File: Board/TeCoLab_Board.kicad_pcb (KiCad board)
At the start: 2 copper layers, 95.1 x 93.8 mm, 61 parts, among them J1 Jack, J2 Supply_Terminal, J3 DC Cooler, Q1 BC337, Q2 TIP122, Q3 TIP122, U1 DS18B20, U2 PC817, U3 DS18B20, U4 DS18B20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

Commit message: PCB: Mounting holes updated to 7 mm. TeCoLab logo resized to 70 percent of the previous size.
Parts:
- removed the G*** at (141.3, 106.6)
- added G***: LOGO, logo:logo, B.Cu at (141.5, 106.2)

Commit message: Schematic: swap of the two labels named Sensor1 and Sensor2. This changes nothing in the PCB layout, but the files were checked as well and saved, generating a new version of them too. Firmware: changed the define of the pin of each sensor, according to the previously mentioned change in the schematic.
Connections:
- A1 pad 11: Sensor_1 -> Sensor_2
- A1 pad 12: Sensor_2 -> Sensor_1
- R5 pad 1: Sensor_2 -> Sensor_1
- R8 pad 1: Sensor_1 -> Sensor_2
- TP6 pad 1: Sensor_1 -> Sensor_2
- TP7 pad 1: Sensor_2 -> Sensor_1
- U3 pad 2: Sensor_2 -> Sensor_1
- U4 pad 2: Sensor_1 -> Sensor_2
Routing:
- net Sensor_2: track 97.9 -> 43.7 mm
- net Sensor_1: track 43.7 -> 97.9 mm
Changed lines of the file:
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@@
       (net 43 "Net-(A1-Pad26)"))
     (pad 11 thru_hole oval (at 0 25.4 180) (size 1.6 1.6) (drill 0.8) (layers *.Cu *.Mask)
-      (net 7 Sensor_1))
+      (net 9 Sensor_2))
     (pad 27 thru_hole oval (at 15.24 7.62 180) (size 1.6 1.6) (drill 0.8) (layers *.Cu *.Mask)
       (net 8 +5V))
     (pad 12 thru_hole oval (at 0 27.94 180) (size 1.6 1.6) (drill 0.8) (layers *.Cu *.Mask)
-      (net 9 Sensor_2))
+      (net 7 Sensor_1))
     (pad 28 thru_hole oval (at 15.24 5.08 180) (size 1.6 1.6) (drill 0.8) (layers *.Cu *.Mask)
       (net 44 "Net-(A1-Pad28)"))
@@
       (net 8 +5V))
     (pad 1 thru_hole circle (at 0 0 90) (size 1.6 1.6) (drill 0.8) (layers *.Cu *.Mask)
-      (net 9 Sensor_2))
+      (net 7 Sensor_1))
     (model ${KISYS3DMOD}/Resistor_THT.3dshapes/R_Axial_DIN0207_L6.3mm_D2.5mm_P7.62mm_Horizontal.wrl
       (at (xyz 0 0 0))
@@
     )
     (pad 1 thru_hole circle (at 0 0 270) (size 1.6 1.6) (drill 0.8) (layers *.Cu *.Mask)
-      (net 7 Sensor_1))
+      (net 9 Sensor_2))
     (pad 2 thru_hole oval (at 7.62 0 270) (size 1.6 1.6) (drill 0.8) (layers *.Cu *.Mask)
       (net 8 +5V))
@@
     (fp_arc (start 1.27 0) (end 1.27 -2.6) (angle 135) (layer F.SilkS) (width 0.12))
     (pad 2 thru_hole oval (at 1.27 0 90) (size 1.05 1.5) (drill 0.75) (layers *.Cu *.Mask)
-      (net 9 Sensor_2))
+      (net 7 Sensor_1))
     (pad 3 thru_hole oval (at 2.54 0 90) (size 1.05 1.5) (drill 0.75) (layers *.Cu *.Mask)
       (net 8 +5V))
@@
       (net 8 +5V))
     (pad 2 thru_hole oval (at 1.27 0 270) (size 1.05 1.5) (drill 0.75) (layers *.Cu *.Mask)
-      (net 7 Sensor_1))
+      (net 9 Sensor_2))
     (model ${KISYS3DMOD}/Package_TO_SOT_THT.3dshapes/TO-92_Inline.wrl
       (at (xyz 0 0 0))
@@
     )
     (pad 1 thru_hole circle (at 0 0) (size 1 1) (drill 0.5) (layers *.Cu *.Mask)
-      (net 7 Sensor_1))
+      (net 9 Sensor_2))
   )
   (module TestPoint:TestPoint_THTPad_D1.0mm_Drill0.5mm (layer F.Cu)
@@
     (fp_circle (center 0 0) (end 0 0.7) (layer F.SilkS) (width 0.12))
     (pad 1 thru_hole circle (at 0 0) (size 1 1) (drill 0.5) (layers *.Cu *.Mask)
-      (net 9 Sensor_2))
+      (net 7 Sensor_1))
   )
   (module MountingHole:MountingHole_6mm (layer F.Cu)
@@
   (segment (start 196.7484 61.77284) (end 191.20108 67.32016) (width 0.2) (layer F.Cu) (net 6))
   (segment (start 196.7484 60.82284) (end 196.7484 61.77284) (width 0.2) (layer F.Cu) (net 6))
-  (segment (start 181.93004 51.36388) (end 181.89956 51.3334) (width 0.2) (layer B.Cu) (net 7))
-  (segment (start 184.7342 51.3334) (end 184.76468 51.36388) (width 0.2) (layer B.Cu) (net 7))
-  (segment (start 181.89956 51.3334) (end 184.7342 51.3334) (width 0.2) (layer B.Cu) (net 7))
-  (segment (start 181.89956 51.3334) (end 179.05476 51.3334) (width 0.2) (layer F.Cu) (net 7))
-  (segment (start 179.05476 51.3334) (end 167.34536 39.624) (width 0.2) (layer F.Cu) (net 7))
-  (segment (start 163.18992 39.624) (end 162.04184 40.77208) (width 0.2) (layer F.Cu) (net 7))
-  (segment (start 167.34536 39.624) (end 163.18992 39.624) (width 0.2) (layer F.Cu) (net 7))
-  (segment (start 161.241841 41.572079) (end 161.221521 41.572079) (width 0.2) (layer F.Cu) (net 7))
-  (segment (start 162.04184 40.77208) (end 161.241841 41.572079) (width 0.2) (layer F.Cu) (net 7))
-  (segment (start 158.21152 44.58208) (end 148.07184 44.58208) (width 0.2) (layer F.Cu) (net 7))
-  (segment (start 161.221521 41.572079) (end 158.21152 44.58208) (width 0.2) (layer F.Cu) (net 7))
+  (segment (start 181.93004 51.36388) (end 181.89956 51.3334) (width 0.2) (layer B.Cu) (net 9))
+  (segment (start 184.7342 51.3334) (end 184.76468 51.36388) (width 0.2) (layer B.Cu) (net 9))
+  (segment (start 181.89956 51.3334) (end 184.7342 51.3334) (width 0.2) (layer B.Cu) (net 9))
+  (segment (start 181.89956 51.3334) (end 179.05476 51.3334) (width 0.2) (layer F.Cu) (net 9))
+  (segment (start 179.05476 51.3334) (end 167.34536 39.624) (width 0.2) (layer F.Cu) (net 9))
+  (segment (start 163.18992 39.624) (end 162.04184 40.77208) (width 0.2) (layer F.Cu) (net 9))
+  (segment (start 167.34536 39.624) (end 163.18992 39.624) (width 0.2) (layer F.Cu) (net 9))
+  (segment (start 161.241841 41.572079) (end 161.221521 41.572079) (width 0.2) (layer F.Cu) (net 9))
+  (segment (start 162.04184 40.77208) (end 161.241841 41.572079) (width 0.2) (layer F.Cu) (net 9))
+  (segment (start 158.21152 44.58208) (end 148.07184 44.58208) (width 0.2) (layer F.Cu) (net 9))
+  (segment (start 161.221521 41.572079) (end 158.21152 44.58208) (width 0.2) (layer F.Cu) (net 9))
   (segment (start 136.92124 50.01768) (end 146.29384 50.01768) (width 0.2) (layer B.Cu) (net 8))
   (segment (start 148.07184 48.23968) (end 148.07184 45.85208) (width 0.2) (layer B.Cu) (net 8) (status 20))
@@
   (segment (start 129.93624 43.31208) (end 134.10184 43.31208) (width 0.2) (layer B.Cu) (net 8))
   (segment (start 128.66624 42.04208) (end 129.93624 43.31208) (width 0.2) (layer B.Cu) (net 8))
-  (segment (start 181.95036 48.7426) (end 181.89956 48.7934) (width 0.2) (layer B.Cu) (net 9))
-  (segment (start 120.63984 48.39208) (end 120.63984 46.97476) (width 0.2) (layer B.Cu) (net 9))
-  (segment (start 123.03252 44.58208) (end 134.10184 44.58208) (width 0.2) (layer B.Cu) (net 9))
-  (segment (start 120.63984 46.97476) (end 123.03252 44.58208) (width 0.2) (layer B.Cu) (net 9))
-  (segment (start 181.92496 48.768) (end 181.89956 48.7934) (width 0.2) (layer B.Cu) (net 9))
-  (segment (start 184.82564 48.768) (end 181.92496 48.768) (width 0.2) (layer B.Cu) (net 9))
-  (segment (start 178.36896 48.7934) (end 181.89956 48.7934) (width 0.2) (layer B.Cu) (net 9))
-  (segment (start 119.85244 37.92728) (end 167.50284 37.92728) (width 0.2) (layer B.Cu) (net 9))
-  (segment (start 118.76024 39.01948) (end 119.85244 37.92728) (width 0.2) (layer B.Cu) (net 9))
-  (segment (start 118.76024 47.89424) (end 118.76024 39.01948) (width 0.2) (layer B.Cu) (net 9))
-  (segment (start 167.50284 37.92728) (end 178.36896 48.7934) (width 0.2) (layer B.Cu) (net 9))
-  (segment (start 119.25808 48.39208) (end 118.76024 47.89424) (width 0.2) (layer B.Cu) (net 9))
-  (segment (start 120.63984 48.39208) (end 119.25808 48.39208) (width 0.2) (layer B.Cu) (net 9))
+  (segment (start 181.95036 48.7426) (end 181.89956 48.7934) (width 0.2) (layer B.Cu) (net 7))
+  (segment (start 120.63984 48.39208) (end 120.63984 46.97476) (width 0.2) (layer B.Cu) (net 7))
+  (segment (start 123.03252 44.58208) (end 134.10184 44.58208) (width 0.2) (layer B.Cu) (net 7))
+  (segment (start 120.63984 46.97476) (end 123.03252 44.58208) (width 0.2) (layer B.Cu) (net 7))
+  (segment (start 181.92496 48.768) (end 181.89956 48.7934) (width 0.2) (layer B.Cu) (net 7))
+  (segment (start 184.82564 48.768) (end 181.92496 48.768) (width 0.2) (layer B.Cu) (net 7))
+  (segment (start 178.36896 48.7934) (end 181.89956 48.7934) (width 0.2) (layer B.Cu) (net 7))
+  (segment (start 119.85244 37.92728) (end 167.50284 37.92728) (width 0.2) (layer B.Cu) (net 7))
+  (segment (start 118.76024 39.01948) (end 119.85244 37.92728) (width 0.2) (layer B.Cu) (net 7))
+  (segment (start 118.76024 47.89424) (end 118.76024 39.01948) (width 0.2) (layer B.Cu) (net 7))
+  (segment (start 167.50284 37.92728) (end 178.36896 48.7934) (width 0.2) (layer B.Cu) (net 7))
+  (segment (start 119.25808 48.39208) (end 118.76024 47.89424) (width 0.2) (layer B.Cu) (net 7))
+  (segment (start 120.63984 48.39208) (end 119.25808 48.39208) (width 0.2) (layer B.Cu) (net 7))
   (segment (start 157.309921 46.069361) (end 157.309921 46.068081) (width 0.2) (layer B.Cu) (net 10))
   (segment (start 158.10992 46.86936) (end 157.309921 46.069361) (width 0.2) (layer B.Cu) (net 10) (status 10))

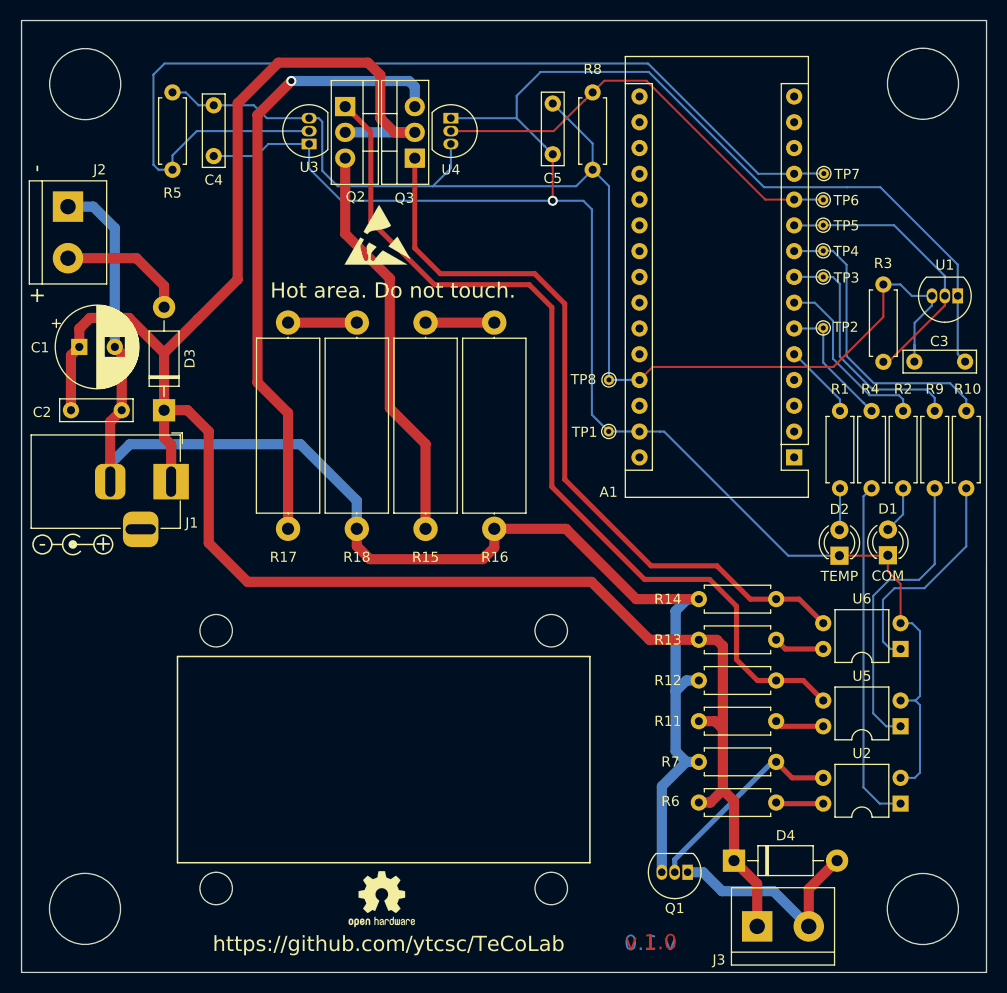
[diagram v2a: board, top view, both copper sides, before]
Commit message: Main Branch Major Update (#19)
* Hardware: Update files to comply with KiCad version 8.0.

* Software: Update dependency handling and experiment logging

- Added requirements.txt for managing Python dependencies
- Updated Manual.tex and Manual.pdf to reflect new setup instructions
- Modified tecolab_experiment.py to handle future pandas concat behavior
- Added rate saturation fields to StepResponse.csv header

* Software: Correct bug where log file was not saving relative setpoint for sensor 2.

* Manual: Remove the manual. Documentation has been moved to the Wiki.

* Software: fix potential unbound variable error when searching serial ports.

* Software: add initial GUI for experiment configuration and real-time plotting.

* Update for KiCad 9.0 compatibility; remove gerbers from repository; Schematic: replaced 10K resistors by 4.7K resistors; PCB: replaced TO-92 package by its hand-soldering version.
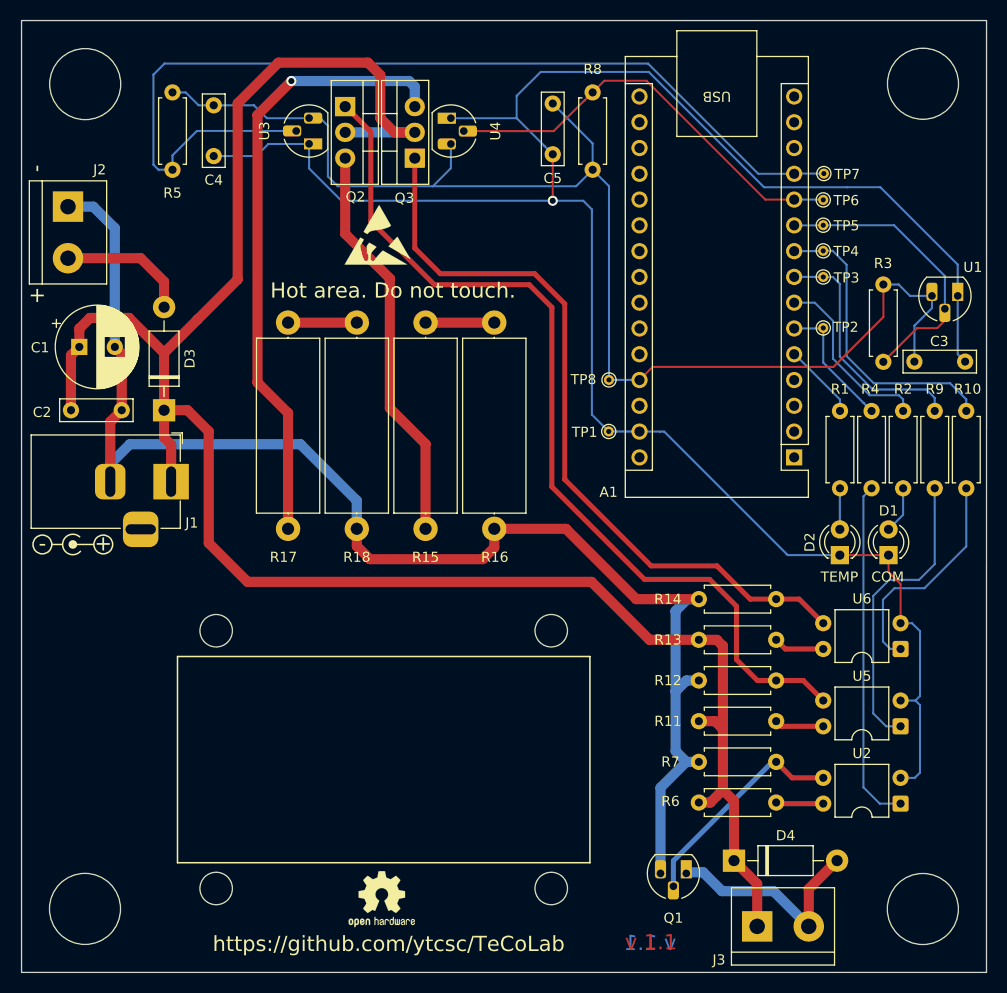
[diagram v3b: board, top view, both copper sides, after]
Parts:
- D1: value COM -> LED
- D2: value TEMP -> LED
- Q1, U1, U3, U4: footprint Package_TO_SOT_THT:TO-92_Inline -> Package_TO_SOT_THT:TO-92_HandSolder
- R3, R5, R7, R8: value 10K -> 4.7K
- moved Q1 0.17 mm to (171.3, 117.7)
- moved D1 0.07 mm to (191.2, 86.4)
- moved D2 0.06 mm to (186.4, 86.4)
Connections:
- net LED_GREEN renamed LED_green
- net LED_RED renamed LED_red
- net RoomTempSensor renamed Sensor_roomtemp
- A1 pad 1: Net-(A1-Pad1) -> unconnected-(A1-D1/TX-Pad1)
- A1 pad 13: Net-(A1-Pad13) -> unconnected-(A1-D10-Pad13)
- A1 pad 14: Net-(A1-Pad14) -> unconnected-(A1-D11-Pad14)
- A1 pad 15: Net-(A1-Pad15) -> unconnected-(A1-D12-Pad15)
- A1 pad 16: Net-(A1-Pad16) -> unconnected-(A1-D13-Pad16)
- A1 pad 17: Net-(A1-Pad17) -> unconnected-(A1-3V3-Pad17)
- A1 pad 18: Net-(A1-Pad18) -> unconnected-(A1-AREF-Pad18)
- A1 pad 19: Net-(A1-Pad19) -> unconnected-(A1-A0-Pad19)
- A1 pad 2: Net-(A1-Pad2) -> unconnected-(A1-D0/RX-Pad2)
- A1 pad 20: Net-(A1-Pad20) -> unconnected-(A1-A1-Pad20)
- A1 pad 21: Net-(A1-Pad21) -> unconnected-(A1-A2-Pad21)
- A1 pad 22: Net-(A1-Pad22) -> unconnected-(A1-A3-Pad22)
- A1 pad 23: Net-(A1-Pad23) -> unconnected-(A1-A4-Pad23)
- A1 pad 24: Net-(A1-Pad24) -> unconnected-(A1-A5-Pad24)
- A1 pad 25: Net-(A1-Pad25) -> unconnected-(A1-A6-Pad25)
- A1 pad 26: Net-(A1-Pad26) -> unconnected-(A1-A7-Pad26)
- A1 pad 28: Net-(A1-Pad28) -> unconnected-(A1-~{RESET}-Pad28)
- A1 pad 3: Net-(A1-Pad3) -> unconnected-(A1-~{RESET}-Pad3)
- A1 pad 30: Net-(A1-Pad30) -> unconnected-(A1-VIN-Pad30)
- A1 pad 4: Net-(A1-Pad4) -> unconnected-(A1-GND-Pad4)
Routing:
- net +5V: track 128.9 -> 130.7 mm
- net Net-(Q1-B): track 20.5 -> 22.0 mm
- net Sensor_roomtemp: track 28.3 -> 29.7 mm
- net Sensor_2: track 43.7 -> 42.4 mm
- net Sensor_1: track 97.9 -> 96.7 mm
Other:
- net class Analog Signals removed
- net class Default removed
- net class Digital Signals removed
- net class Power removed
- board text added: "COM"
- board text added: "TEMP"
- board text added: "v 1.1"
- board text removed: "v 1.0"
